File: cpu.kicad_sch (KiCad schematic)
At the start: 22 parts, among them IC1 68HC000, IC2 LHP6323, IC7 MSM54C864

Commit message: Additional power/reset switches for Neptune case.
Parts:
- C912: footprint Capacitor_THT:CP_Radial_D5.0mm_P2.50mm -> Neptune:CP_Radial_D5.0mm_P2.50mm_Horizontal
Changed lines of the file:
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@@
       (effects (font (size 1.27 1.27)) (justify left))
     )
-    (property "Footprint" "Capacitor_THT:CP_Radial_D5.0mm_P2.50mm" (at 310.1848 159.766 0)
+    (property "Footprint" "Neptune:CP_Radial_D5.0mm_P2.50mm_Horizontal" (at 310.1848 159.766 0)
       (effects (font (size 1.27 1.27)) hide)
     )

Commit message: General tweaks, add some DigiKey part numbers.
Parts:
- CA601, CA602, CA603, CA604: DigiKey (none) -> 13-CA0612KRNPO9BN330CT-ND
- R3: DigiKey (none) -> P220CCT-ND
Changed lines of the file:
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@@
+      (effects (font (size 1.27 1.27)) hide)
+    )
+    (property "DigiKey" "13-CA0612KRNPO9BN330CT-ND" (at 140.97 231.14 0)
       (effects (font (size 1.27 1.27)) hide)
     )
@@
       (effects (font (size 1.27 1.27)) hide)
     )
+    (property "DigiKey" "" (at 323.85 155.956 0)
+      (effects (font (size 1.27 1.27)) hide)
+    )
     (pin "1")
     (pin "2")
@@
     )
     (property "Datasheet" "https://www.nxp.com/docs/en/reference-manual/MC68000UM.pdf" (at 166.37 115.57 0)
+      (effects (font (size 1.27 1.27)) hide)
+    )
+    (property "DigiKey" "" (at 166.37 115.57 0)
       (effects (font (size 1.27 1.27)) hide)
     )
@@
       (effects (font (size 1.27 1.27)) hide)
     )
+    (property "DigiKey" "" (at 65.405 231.14 0)
+      (effects (font (size 1.27 1.27)) hide)
+    )
     (pin "1")
     (pin "2")
@@
     )
     (property "Datasheet" "" (at 302.26 196.85 0)
+      (effects (font (size 1.27 1.27)) hide)
+    )
+    (property "DigiKey" "" (at 301.625 193.675 0)
       (effects (font (size 1.27 1.27)) hide)
     )
@@
       (effects (font (size 1.27 1.27)) hide)
     )
+    (property "DigiKey" "" (at 349.885 216.535 0)
+      (effects (font (size 1.27 1.27)) hide)
+    )
     (pin "1")
     (pin "2")
@@
       (effects (font (size 1.27 1.27)) hide)
     )
+    (property "DigiKey" "P220CCT-ND" (at 196.85 163.83 0)
+      (effects (font (size 1.27 1.27)) hide)
+    )
     (pin "1")
     (pin "2")
@@
     )
     (property "Datasheet" "~" (at 333.375 216.535 0)
+      (effects (font (size 1.27 1.27)) hide)
+    )
+    (property "DigiKey" "" (at 333.375 216.535 0)
       (effects (font (size 1.27 1.27)) hide)
     )
@@
     )
     (property "Datasheet" "~" (at 101.6 231.14 0)
+      (effects (font (size 1.27 1.27)) hide)
+    )
+    (property "DigiKey" "13-CA0612KRNPO9BN330CT-ND" (at 102.87 231.14 0)
       (effects (font (size 1.27 1.27)) hide)
     )
@@
       (effects (font (size 1.27 1.27)) hide)
     )
+    (property "DigiKey" "" (at 135.255 133.35 0)
+      (effects (font (size 1.27 1.27)) hide)
+    )
     (pin "1")
     (pin "2")
@@
       (effects (font (size 1.27 1.27)) hide)
     )
+    (property "DigiKey" "" (at 358.14 216.535 0)
+      (effects (font (size 1.27 1.27)) hide)
+    )
     (pin "1")
     (pin "2")
@@
     )
     (property "Datasheet" "~" (at 295.91 60.96 0)
+      (effects (font (size 1.27 1.27)) hide)
+    )
+    (property "DigiKey" "" (at 295.91 60.96 0)
       (effects (font (size 1.27 1.27)) hide)
     )
@@
       (effects (font (size 1.27 1.27)) hide)
     )
+    (property "DigiKey" "" (at 341.63 216.535 0)
+      (effects (font (size 1.27 1.27)) hide)
+    )
     (pin "1")
     (pin "2")
@@
     )
     (property "Datasheet" "~" (at 311.15 155.956 0)
+      (effects (font (size 1.27 1.27)) hide)
+    )
+    (property "DigiKey" "" (at 311.15 155.956 0)
       (effects (font (size 1.27 1.27)) hide)
     )
@@
     )
     (property "Datasheet" "~" (at 121.92 231.14 0)
+      (effects (font (size 1.27 1.27)) hide)
+    )
+    (property "DigiKey" "13-CA0612KRNPO9BN330CT-ND" (at 123.19 231.14 0)
       (effects (font (size 1.27 1.27)) hide)
     )
@@
       (effects (font (size 1.27 1.27)) hide)
     )
+    (property "DigiKey" "" (at 271.145 111.76 0)
+      (effects (font (size 1.27 1.27)) hide)
+    )
     (pin "1")
     (pin "2")
@@
     )
     (property "Datasheet" "~" (at 161.925 231.14 0)
+      (effects (font (size 1.27 1.27)) hide)
+    )
+    (property "DigiKey" "13-CA0612KRNPO9BN330CT-ND" (at 163.195 231.14 0)
       (effects (font (size 1.27 1.27)) hide)
     )
@@
       (effects (font (size 1.27 1.27)) hide)
     )
+    (property "DigiKey" "" (at 285.115 111.76 0)
+      (effects (font (size 1.27 1.27)) hide)
+    )
     (pin "1")
     (pin "2")
@@
     )
     (property "Datasheet" "" (at 249.555 76.835 0)
+      (effects (font (size 1.27 1.27)) hide)
+    )
+    (property "DigiKey" "" (at 249.555 76.835 0)
       (effects (font (size 1.27 1.27)) hide)
     )
@@
       (effects (font (size 1.27 1.27)) hide)
     )
+    (property "DigiKey" "" (at 135.255 59.69 0)
+      (effects (font (size 1.27 1.27)) hide)
+    )
     (pin "1")
     (pin "2")
@@
       (effects (font (size 1.27 1.27)) hide)
     )
+    (property "DigiKey" "" (at 102.235 55.88 0)
+      (effects (font (size 1.27 1.27)) hide)
+    )
     (pin "1")
     (pin "2")
@@
       (effects (font (size 1.27 1.27)) hide)
     )
+    (property "DigiKey" "" (at 89.535 55.88 0)
+      (effects (font (size 1.27 1.27)) hide)
+    )

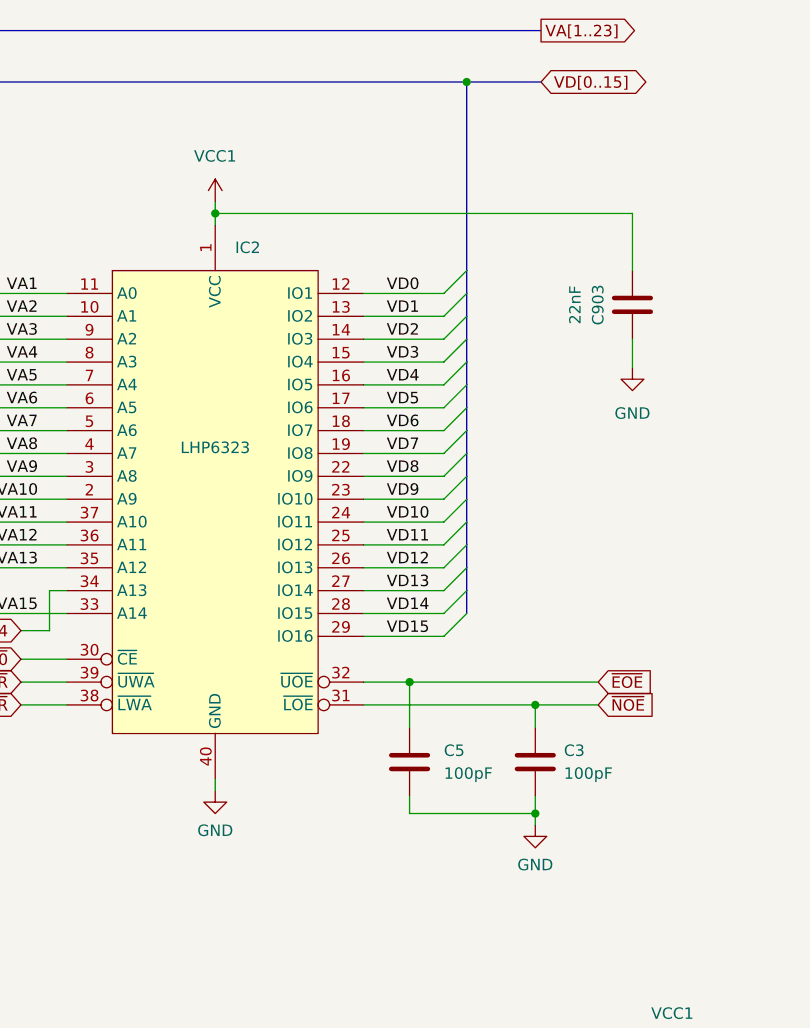
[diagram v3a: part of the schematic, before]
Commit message: Fix power routing for IC2.
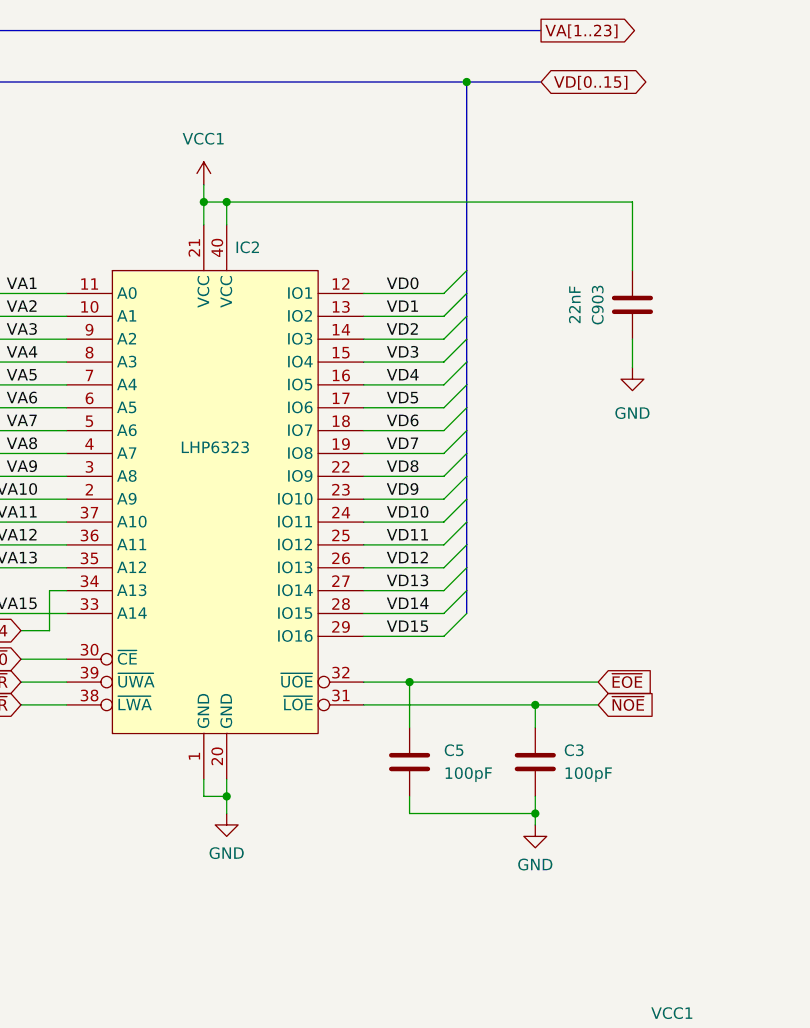
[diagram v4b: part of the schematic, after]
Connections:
- net GND: now also IC2.1 (GND), IC2.20 (GND); no longer IC2.40 (GND)
- net VCC1: now also IC2.21 (VCC), IC2.40 (VCC); no longer IC2.1 (VCC)
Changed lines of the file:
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@@
   (junction (at 358.14 201.93) (diameter 0) (color 0 0 0 0)
   )
+  (junction (at 250.825 115.57) (diameter 0) (color 0 0 0 0)
+  )
   (junction (at 341.63 222.885) (diameter 0) (color 0 0 0 0)
   )
@@
   (junction (at 116.205 67.31) (diameter 0) (color 0 0 0 0)
   )
+  (junction (at 250.825 49.53) (diameter 0) (color 0 0 0 0)
+  )
   (junction (at 118.11 241.3) (diameter 0) (color 0 0 0 0)
   )
@@
   (junction (at 140.97 241.3) (diameter 0) (color 0 0 0 0)
   )
-  (junction (at 249.555 50.8) (diameter 0) (color 0 0 0 0)
-  )
   (junction (at 120.65 241.3) (diameter 0) (color 0 0 0 0)
   )
@@
   )
   (junction (at 333.375 209.55) (diameter 0) (color 0 0 0 0)
+  )
+  (junction (at 248.285 49.53) (diameter 0) (color 0 0 0 0)
   )
   (junction (at 285.115 117.475) (diameter 0) (color 0 0 0 0)
@@
     (stroke (width 0) (type default))
   )
-  (wire (pts (xy 295.91 57.15) (xy 295.91 50.8))
+  (wire (pts (xy 295.91 57.15) (xy 295.91 49.53))
     (stroke (width 0) (type default))
   )
@@
     (stroke (width 0) (type default))
   )
-  (wire (pts (xy 295.91 50.8) (xy 249.555 50.8))
-    (stroke (width 0) (type default))
-  )
   (wire (pts (xy 274.955 206.375) (xy 286.385 206.375))
     (stroke (width 0) (type default))
@@
     (stroke (width 0) (type default))
   )
+  (wire (pts (xy 250.825 115.57) (xy 250.825 117.475))
+    (stroke (width 0) (type default))
+  )
   (wire (pts (xy 274.955 180.975) (xy 286.385 180.975))
     (stroke (width 0) (type default))
@@
     (stroke (width 0) (type default))
   )
+  (wire (pts (xy 250.825 113.665) (xy 250.825 115.57))
+    (stroke (width 0) (type default))
+  )
   (wire (pts (xy 274.955 173.355) (xy 286.385 173.355))
     (stroke (width 0) (type default))
@@
     (stroke (width 0) (type default))
   )
-  (wire (pts (xy 249.555 113.665) (xy 249.555 114.935))
-    (stroke (width 0) (type default))
-  )
   (wire (pts (xy 191.77 171.45) (xy 201.93 171.45))
     (stroke (width 0) (type default))
@@
     (stroke (width 0) (type default))
   )
-  (wire (pts (xy 249.555 49.53) (xy 249.555 50.8))
+  (wire (pts (xy 248.285 47.625) (xy 248.285 49.53))
     (stroke (width 0) (type default))
   )
@@
     (stroke (width 0) (type default))
   )
+  (wire (pts (xy 248.285 115.57) (xy 250.825 115.57))
+    (stroke (width 0) (type default))
+  )
   (bus (pts (xy 220.98 82.55) (xy 220.98 80.01))
     (stroke (width 0) (type default))
@@
     (stroke (width 0) (type default))
   )
-  (wire (pts (xy 249.555 50.8) (xy 249.555 52.07))
-    (stroke (width 0) (type default))
-  )
   (wire (pts (xy 138.43 236.22) (xy 138.43 241.3))
     (stroke (width 0) (type default))
@@
     (stroke (width 0) (type default))
   )
+  (wire (pts (xy 250.825 49.53) (xy 250.825 52.07))
+    (stroke (width 0) (type default))
+  )
+  (wire (pts (xy 250.825 49.53) (xy 295.91 49.53))
+    (stroke (width 0) (type default))
+  )
   (bus (pts (xy 203.2 97.79) (xy 203.2 95.25))
     (stroke (width 0) (type default))
@@
     (stroke (width 0) (type default))
   )
+  (wire (pts (xy 248.285 49.53) (xy 248.285 52.07))
+    (stroke (width 0) (type default))
+  )
   (bus (pts (xy 277.495 36.195) (xy 285.75 36.195))
     (stroke (width 0) (type default))
@@
     (stroke (width 0) (type default))
   )
+  (wire (pts (xy 248.285 113.665) (xy 248.285 115.57))
+    (stroke (width 0) (type default))
+  )
   (wire (pts (xy 191.77 90.17) (xy 200.66 90.17))
     (stroke (width 0) (type default))
@@
   )
   (wire (pts (xy 118.11 241.3) (xy 120.65 241.3))
+    (stroke (width 0) (type default))
+  )
+  (wire (pts (xy 248.285 49.53) (xy 250.825 49.53))
     (stroke (width 0) (type default))
   )
@@
     )
   )
-  (symbol (lib_id "MegaDrive:VCC1") (at 249.555 49.53 0) (unit 1)
+  (symbol (lib_id "MegaDrive:VCC1") (at 248.285 47.625 0) (unit 1)
     (in_bom yes) (on_board yes) (dnp no) (fields_autoplaced)
-    (property "Reference" "#PWR01" (at 249.555 53.34 0)
-      (effects (font (size 1.27 1.27)) hide)
-    )
-    (property "Value" "VCC1" (at 249.555 44.45 0)
+    (property "Reference" "#PWR01" (at 248.285 51.435 0)
+      (effects (font (size 1.27 1.27)) hide)
+    )
+    (property "Value" "VCC1" (at 248.285 42.545 0)
       (effects (font (size 1.27 1.27)))
     )
-    (property "Footprint" "" (at 249.555 49.53 0)
-      (effects (font (size 1.27 1.27)) hide)
-    )
-    (property "Datasheet" "" (at 249.555 49.53 0)
+    (property "Footprint" "" (at 248.285 47.625 0)
+      (effects (font (size 1.27 1.27)) hide)
+    )
+    (property "Datasheet" "" (at 248.285 47.625 0)
       (effects (font (size 1.27 1.27)) hide)
     )
@@
     )
   )
-  (symbol (lib_id "power:GND") (at 249.555 114.935 0) (unit 1)
+  (symbol (lib_id "power:GND") (at 250.825 117.475 0) (unit 1)
     (in_bom yes) (on_board yes) (dnp no) (fields_autoplaced)
-    (property "Reference" "#PWR02" (at 249.555 121.285 0)
-      (effects (font (size 1.27 1.27)) hide)
-    )
-    (property "Value" "GND" (at 249.555 119.38 0)
+    (property "Reference" "#PWR02" (at 250.825 123.825 0)
+      (effects (font (size 1.27 1.27)) hide)
+    )
+    (property "Value" "GND" (at 250.825 121.92 0)
       (effects (font (size 1.27 1.27)))
     )
-    (property "Footprint" "" (at 249.555 114.935 0)
-      (effects (font (size 1.27 1.27)) hide)
-    )
-    (property "Datasheet" "" (at 249.555 114.935 0)
+    (property "Footprint" "" (at 250.825 117.475 0)
+      (effects (font (size 1.27 1.27)) hide)
+    )
+    (property "Datasheet" "" (at 250.825 117.475 0)
       (effects (font (size 1.27 1.27)) hide)
     )
@@
     (pin "19")
     (pin "2")
+    (pin "20")
+    (pin "21")
     (pin "22")
     (pin "23")
